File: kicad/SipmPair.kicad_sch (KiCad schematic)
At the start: 26 parts, among them J12 Conn_Coaxial, J13 Conn_Coaxial, U12 OPA847IDBVT, U13 OPA847IDBVT

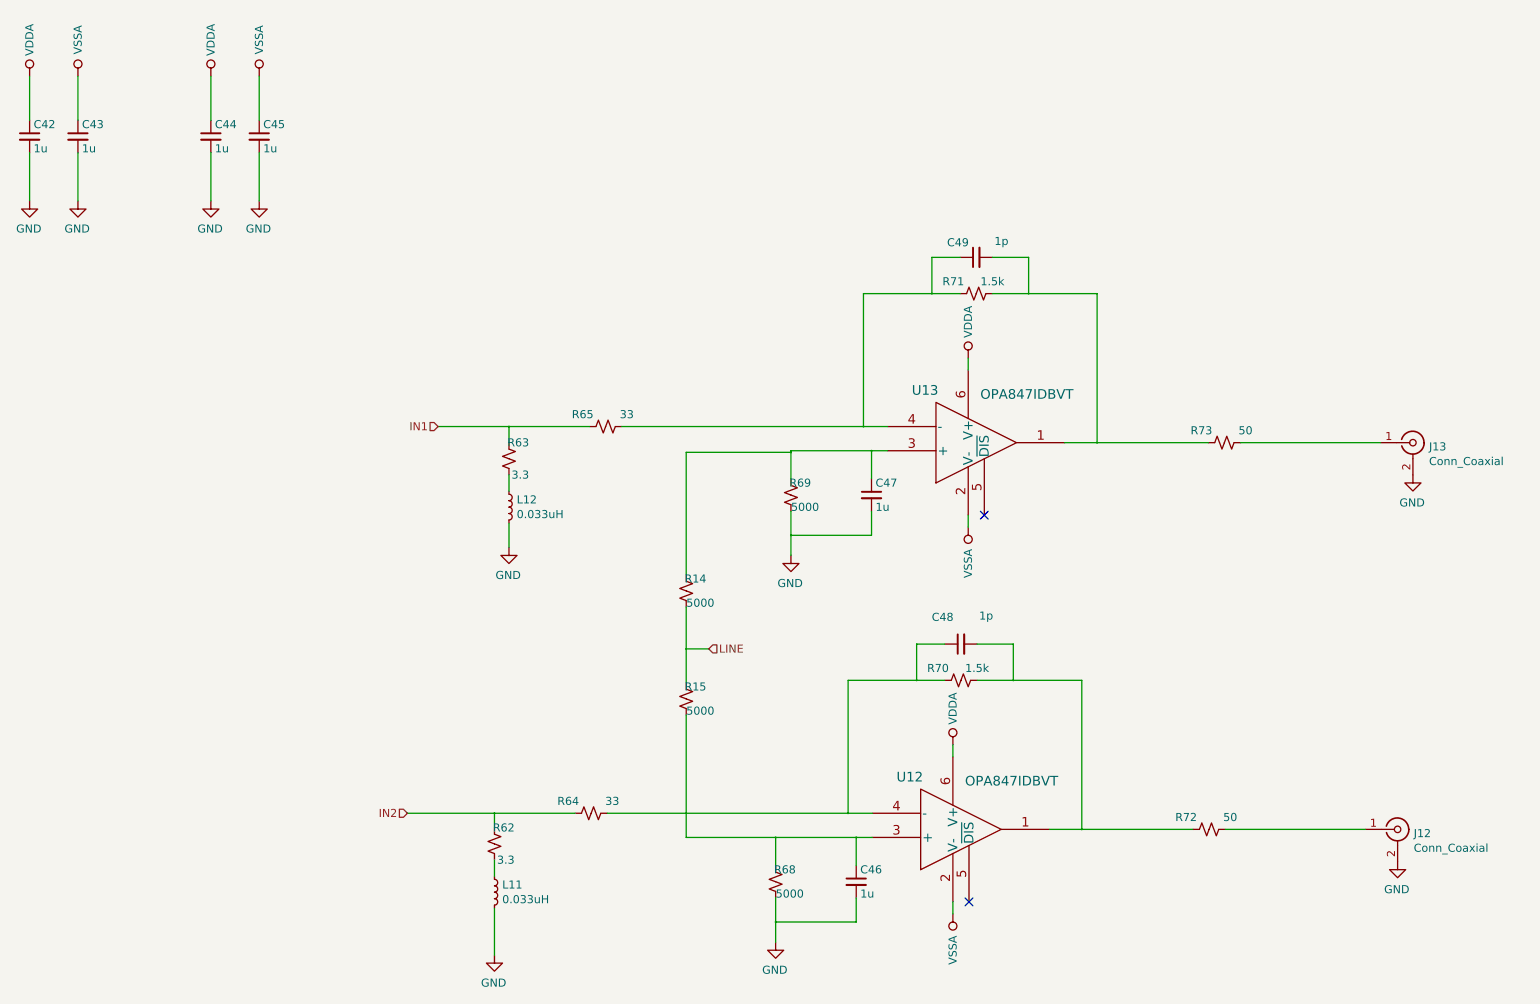
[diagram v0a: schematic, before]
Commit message: Update layout for the new footprint
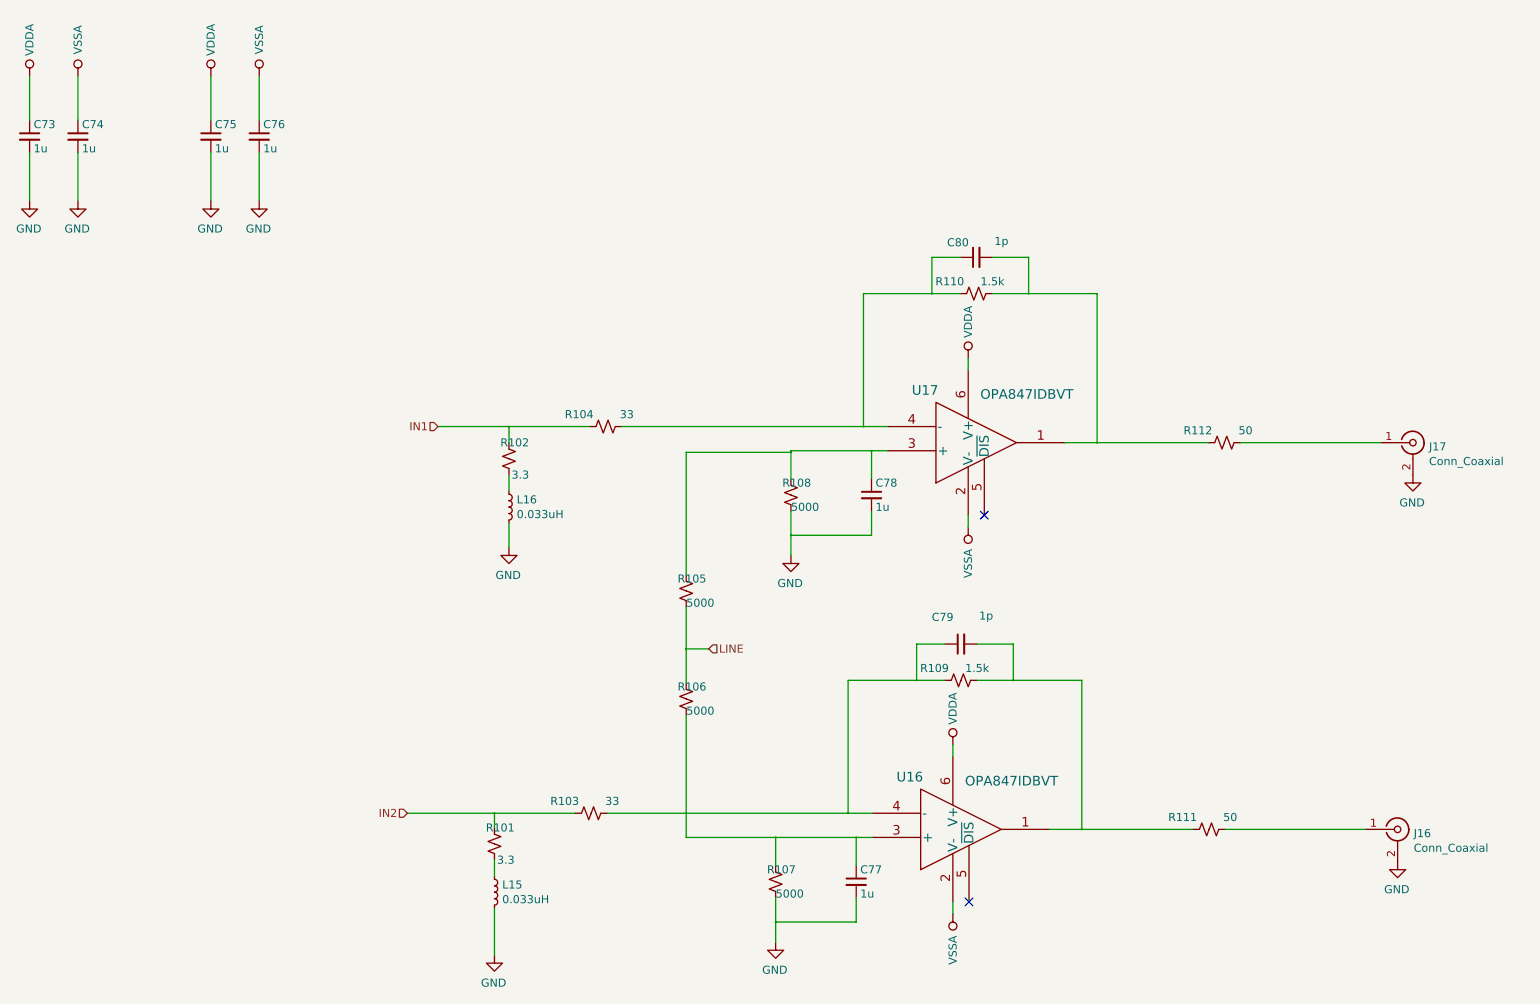
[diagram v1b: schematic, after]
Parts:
- renumbered C42 to C73, C43 to C74, C44 to C75, C45 to C76, C46 to C77, C47 to C78, C48 to C79, C49 to C80, J12 to J16, J13 to J17, L11 to L15, L12 to L16, R62 to R101, R63 to R102, R64 to R103, R65 to R104, R14 to R105, R15 to R106, R68 to R107, R69 to R108, R70 to R109, R71 to R110, R72 to R111, R73 to R112, U12 to U16, U13 to U17

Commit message: Update foot print for the revised hamamatsu part
They only have 2 cathode connections.  In addition, add a second power connector, since at least two power supplies are going to be needed.
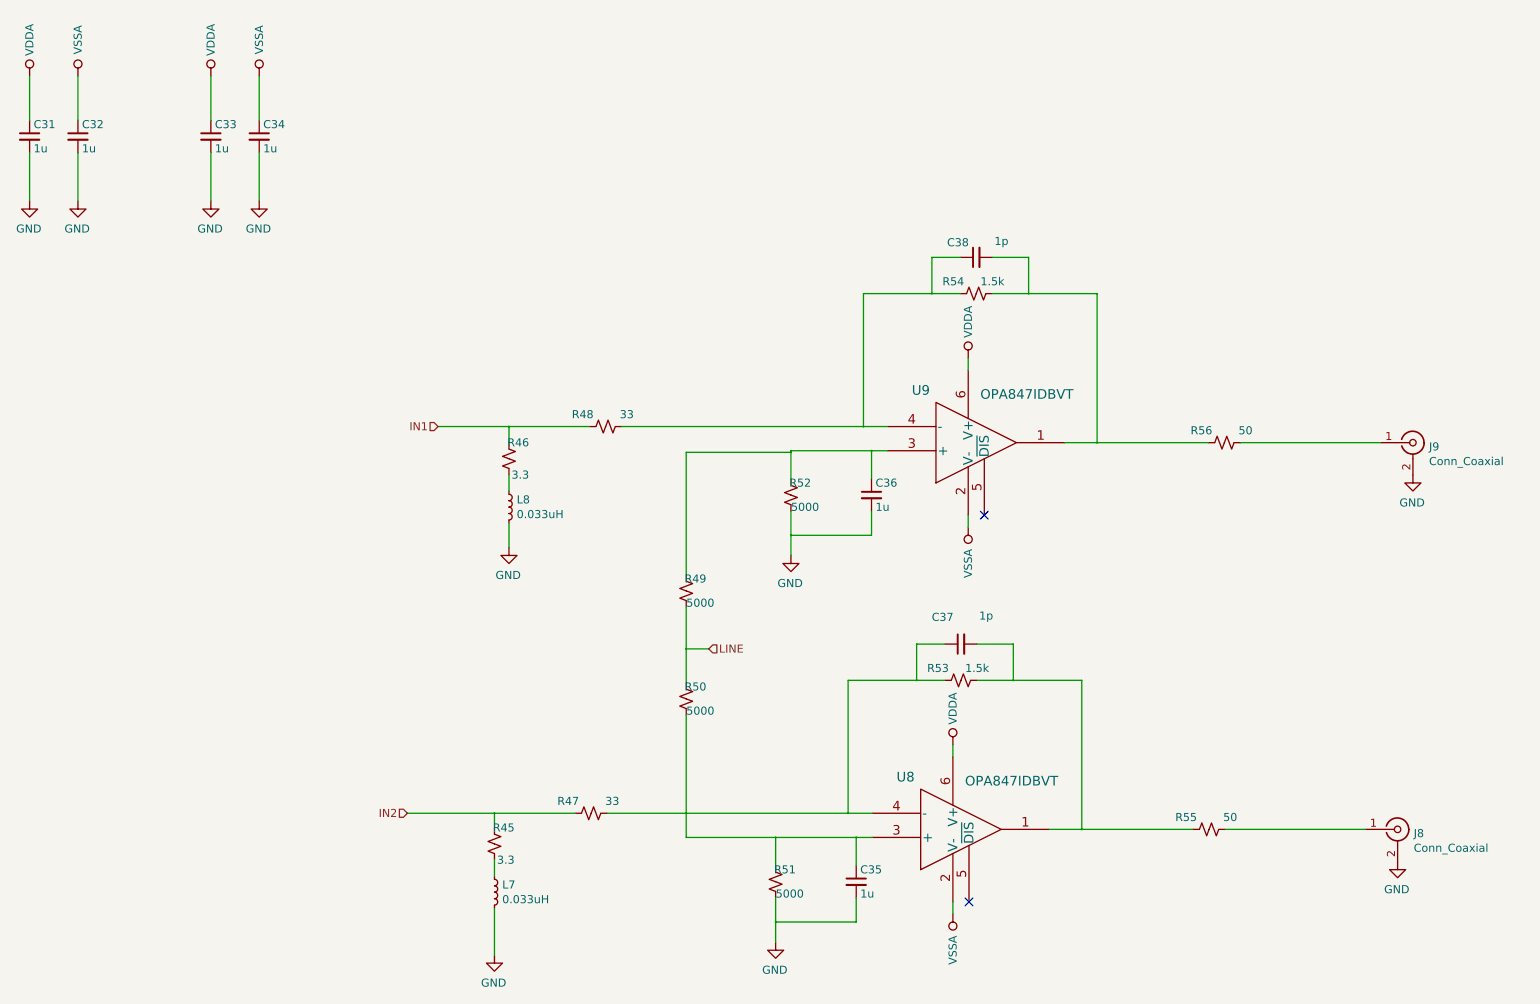
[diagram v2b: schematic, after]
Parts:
- renumbered C73 to C31, C74 to C32, C75 to C33, C76 to C34, C77 to C35, C78 to C36, C79 to C37, C80 to C38, J16 to J8, J17 to J9, L15 to L7, L16 to L8, R101 to R45, R102 to R46, R103 to R47, R104 to R48, R105 to R49, R106 to R50, R107 to R51, R108 to R52, R109 to R53, R110 to R54, R111 to R55, R112 to R56, U16 to U8, U17 to U9
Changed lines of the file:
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@@
   (symbol (lib_id "Device:L_Small") (at 101.854 153.416 0)
     (in_bom yes) (on_board yes)
-    (property "Reference" "L15" (id 0) (at 103.0732 152.2476 0)
+    (property "Reference" "L7" (id 0) (at 103.0732 152.2476 0)
       (effects (font (size 1.27 1.27)) (justify left))
     )
@@
   (symbol (lib_id "Device:L_Small") (at 104.14 92.71 0)
     (in_bom yes) (on_board yes)
-    (property "Reference" "L16" (id 0) (at 105.3592 91.5416 0)
+    (property "Reference" "L8" (id 0) (at 105.3592 91.5416 0)
       (effects (font (size 1.27 1.27)) (justify left))
     )
@@
   (symbol (lib_id "Device:R_Small_US") (at 101.854 145.796 180)
     (in_bom yes) (on_board yes)
-    (property "Reference" "R101" (id 0) (at 105.029 143.256 0)
+    (property "Reference" "R45" (id 0) (at 105.029 143.256 0)
       (effects (font (size 1.27 1.27)) (justify left))
     )
@@
   (symbol (lib_id "Device:R_Small_US") (at 104.14 85.09 180)
     (in_bom yes) (on_board yes)
-    (property "Reference" "R102" (id 0) (at 107.315 82.55 0)
+    (property "Reference" "R46" (id 0) (at 107.315 82.55 0)
       (effects (font (size 1.27 1.27)) (justify left))
     )
@@
   (symbol (lib_id "Device:R_Small_US") (at 117.094 140.97 90)
     (in_bom yes) (on_board yes)
-    (property "Reference" "R103" (id 0) (at 115.189 139.065 90)
+    (property "Reference" "R47" (id 0) (at 115.189 139.065 90)
       (effects (font (size 1.27 1.27)) (justify left))
     )
@@
   (symbol (lib_id "Device:R_Small_US") (at 119.38 80.01 90)
     (in_bom yes) (on_board yes)
-    (property "Reference" "R104" (id 0) (at 117.475 78.105 90)
+    (property "Reference" "R48" (id 0) (at 117.475 78.105 90)
       (effects (font (size 1.27 1.27)) (justify left))
     )
@@
   (symbol (lib_id "Device:R_Small_US") (at 132.08 105.918 180)
     (in_bom yes) (on_board yes)
-    (property "Reference" "R105" (id 0) (at 135.255 104.013 0)
+    (property "Reference" "R49" (id 0) (at 135.255 104.013 0)
       (effects (font (size 1.27 1.27)) (justify left))
     )
@@
   (symbol (lib_id "Device:R_Small_US") (at 132.08 122.936 180)
     (in_bom yes) (on_board yes)
-    (property "Reference" "R106" (id 0) (at 135.255 121.031 0)
+    (property "Reference" "R50" (id 0) (at 135.255 121.031 0)
       (effects (font (size 1.27 1.27)) (justify left))
     )
@@
   (symbol (lib_id "Device:R_Small_US") (at 146.177 151.765 180)
     (in_bom yes) (on_board yes)
-    (property "Reference" "R107" (id 0) (at 149.352 149.86 0)
+    (property "Reference" "R51" (id 0) (at 149.352 149.86 0)
       (effects (font (size 1.27 1.27)) (justify left))
     )
@@
   (symbol (lib_id "Device:R_Small_US") (at 148.59 90.805 180)
     (in_bom yes) (on_board yes)
-    (property "Reference" "R108" (id 0) (at 151.765 88.9 0)
+    (property "Reference" "R52" (id 0) (at 151.765 88.9 0)
       (effects (font (size 1.27 1.27)) (justify left))
     )
@@
   (symbol (lib_id "Device:R_Small_US") (at 175.387 120.015 90)
     (in_bom yes) (on_board yes)
-    (property "Reference" "R109" (id 0) (at 173.482 118.11 90)
+    (property "Reference" "R53" (id 0) (at 173.482 118.11 90)
       (effects (font (size 1.27 1.27)) (justify left))
     )
@@
   (symbol (lib_id "Device:R_Small_US") (at 177.8 59.055 90)
     (in_bom yes) (on_board yes)
-    (property "Reference" "R110" (id 0) (at 175.895 57.15 90)
+    (property "Reference" "R54" (id 0) (at 175.895 57.15 90)
       (effects (font (size 1.27 1.27)) (justify left))
     )
@@
   (symbol (lib_id "Device:R_Small_US") (at 214.503 143.51 90)
     (in_bom yes) (on_board yes)
-    (property "Reference" "R111" (id 0) (at 212.598 141.605 90)
+    (property "Reference" "R55" (id 0) (at 212.598 141.605 90)
       (effects (font (size 1.27 1.27)) (justify left))
     )
@@
   (symbol (lib_id "Device:R_Small_US") (at 216.916 82.55 90)
     (in_bom yes) (on_board yes)
-    (property "Reference" "R112" (id 0) (at 215.011 80.645 90)
+    (property "Reference" "R56" (id 0) (at 215.011 80.645 90)
       (effects (font (size 1.27 1.27)) (justify left))
     )
@@
   (symbol (lib_id "Device:C_Small") (at 28.575 34.29 0)
     (in_bom yes) (on_board yes)
-    (property "Reference" "C73" (id 0) (at 29.21 32.385 0)
+    (property "Reference" "C31" (id 0) (at 29.21 32.385 0)
       (effects (font (size 1.27 1.27)) (justify left))
     )
@@
   (symbol (lib_id "Device:C_Small") (at 36.195 34.29 0)
     (in_bom yes) (on_board yes)
-    (property "Reference" "C74" (id 0) (at 36.83 32.385 0)
+    (property "Reference" "C32" (id 0) (at 36.83 32.385 0)
       (effects (font (size 1.27 1.27)) (justify left))
     )
@@
   (symbol (lib_id "Device:C_Small") (at 57.15 34.29 0)
     (in_bom yes) (on_board yes)
-    (property "Reference" "C75" (id 0) (at 57.785 32.385 0)
+    (property "Reference" "C33" (id 0) (at 57.785 32.385 0)
       (effects (font (size 1.27 1.27)) (justify left))
     )
@@
   (symbol (lib_id "Device:C_Small") (at 64.77 34.29 0)
     (in_bom yes) (on_board yes)
-    (property "Reference" "C76" (id 0) (at 65.405 32.385 0)
+    (property "Reference" "C34" (id 0) (at 65.405 32.385 0)
       (effects (font (size 1.27 1.27)) (justify left))
     )
@@
   (symbol (lib_id "Device:C_Small") (at 158.877 151.765 0)
     (in_bom yes) (on_board yes)
-    (property "Reference" "C77" (id 0) (at 159.512 149.86 0)
+    (property "Reference" "C35" (id 0) (at 159.512 149.86 0)
       (effects (font (size 1.27 1.27)) (justify left))
     )
@@
   (symbol (lib_id "Device:C_Small") (at 161.29 90.805 0)
     (in_bom yes) (on_board yes)
-    (property "Reference" "C78" (id 0) (at 161.925 88.9 0)
+    (property "Reference" "C36" (id 0) (at 161.925 88.9 0)
       (effects (font (size 1.27 1.27)) (justify left))
     )
@@
   (symbol (lib_id "Device:C_Small") (at 175.387 114.3 90)
     (in_bom yes) (on_board yes)
-    (property "Reference" "C79" (id 0) (at 174.2186 110.0582 90)
+    (property "Reference" "C37" (id 0) (at 174.2186 110.0582 90)
       (effects (font (size 1.27 1.27)) (justify left))
     )
@@
   (symbol (lib_id "Device:C_Small") (at 177.8 53.34 90)
     (in_bom yes) (on_board yes)
-    (property "Reference" "C80" (id 0) (at 176.6316 51.0032 90)
+    (property "Reference" "C38" (id 0) (at 176.6316 51.0032 90)
       (effects (font (size 1.27 1.27)) (justify left))
     )
@@
   (symbol (lib_id "Connector:Conn_Coaxial") (at 244.221 143.51 0)
     (in_bom yes) (on_board yes)
-    (property "Reference" "J16" (id 0) (at 246.761 144.145 0)
+    (property "Reference" "J8" (id 0) (at 246.761 144.145 0)
       (effects (font (size 1.27 1.27)) (justify left))
     )
@@
   (symbol (lib_id "Connector:Conn_Coaxial") (at 246.634 82.55 0)
     (in_bom yes) (on_board yes)
-    (property "Reference" "J17" (id 0) (at 249.174 83.185 0)
+    (property "Reference" "J9" (id 0) (at 249.174 83.185 0)
       (effects (font (size 1.27 1.27)) (justify left))
     )
@@
   (symbol (lib_id "OPA847:OPA847IDBVT") (at 160.147 175.26 0)
     (in_bom yes) (on_board yes)
-    (property "Reference" "U16" (id 0) (at 165.227 135.255 0)
+    (property "Reference" "U8" (id 0) (at 165.227 135.255 0)
       (effects (font (size 1.524 1.524)) (justify left))
     )
@@
   (symbol (lib_id "OPA847:OPA847IDBVT") (at 162.56 114.3 0)
     (in_bom yes) (on_board yes)
-    (property "Reference" "U17" (id 0) (at 167.64 74.295 0)
+    (property "Reference" "U9" (id 0) (at 167.64 74.295 0)
       (effects (font (size 1.524 1.524)) (justify left))
     )

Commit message: Split power rails across two power supplies
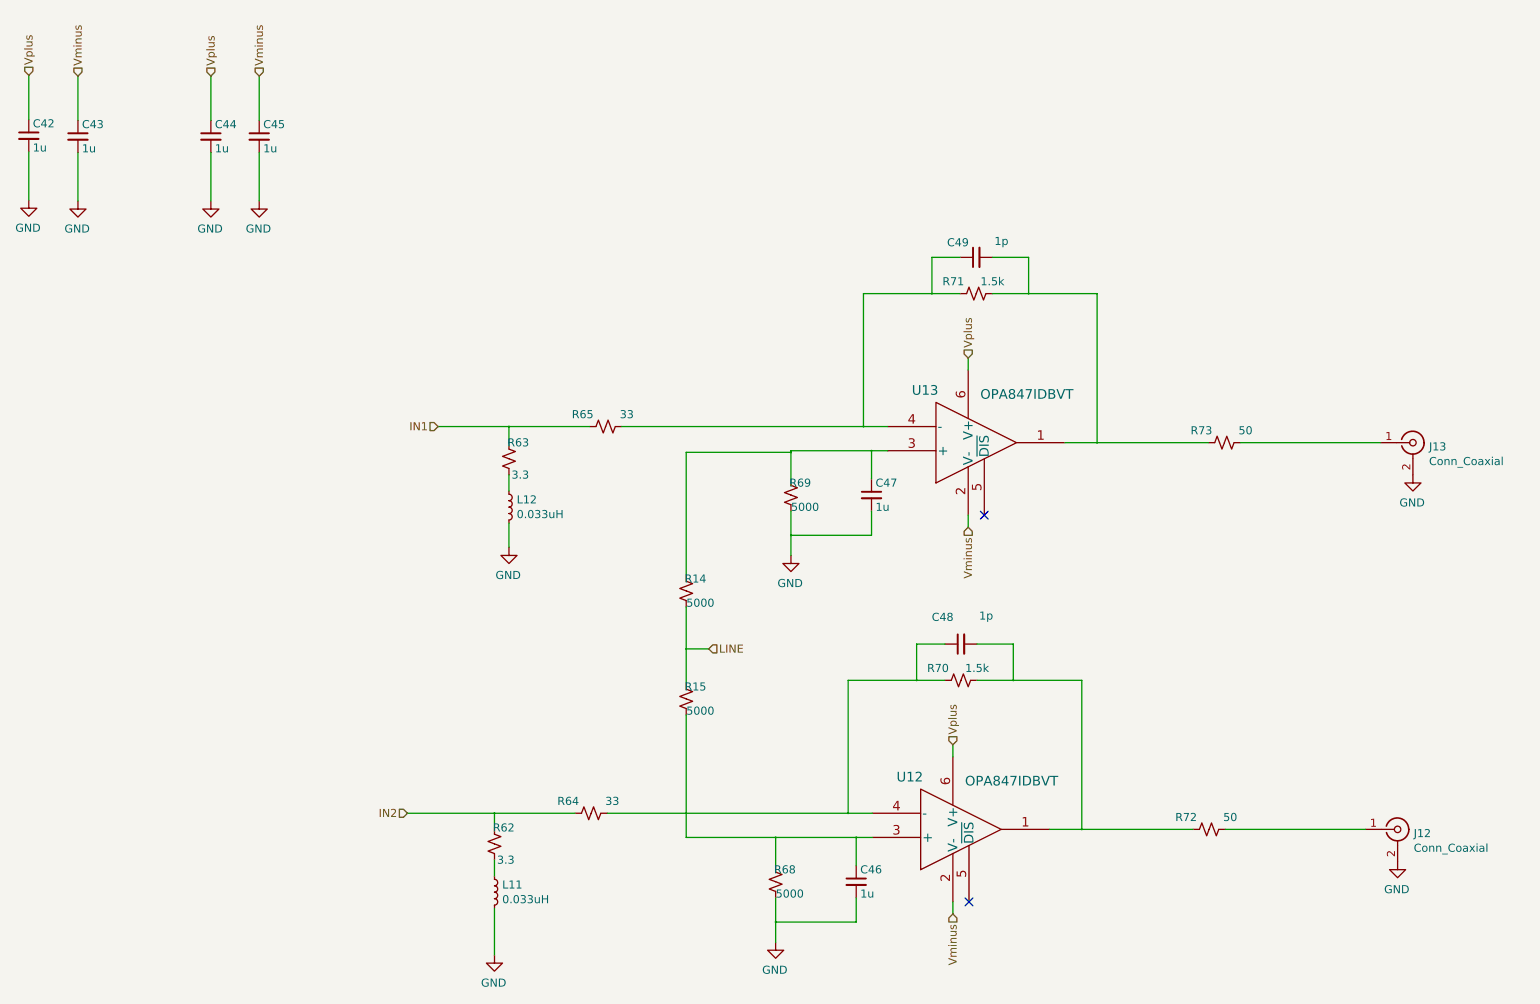
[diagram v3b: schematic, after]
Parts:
- renumbered C31 to C42, C32 to C43, C33 to C44, C34 to C45, C35 to C46, C36 to C47, C37 to C48, C38 to C49, J8 to J12, J9 to J13, L7 to L11, L8 to L12, R49 to R14, R50 to R15, R45 to R62, R46 to R63, R47 to R64, R48 to R65, R51 to R68, R52 to R69, R53 to R70, R54 to R71, R55 to R72, R56 to R73, U8 to U12, U9 to U13
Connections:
- net VDDA renamed Vplus
- net VSSA renamed Vminus
